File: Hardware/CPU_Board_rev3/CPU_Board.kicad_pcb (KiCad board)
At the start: 2 copper layers, 100 x 70 mm, 116 parts, among them P1 CONN_01X02, P10 CONN_01X02, P11 CONN_01X06, P12 CONN_01X03, P13 CONN_01X01, P14 CONN_01X03, P15 CONN_01X01, P16 CONN_01X01, P17 CONN_01X01, P18 CONN_01X03, P19 CONN_01X01, P2 USB_B, P20 CONN_01X01, P21 CONN_01X06, P22 CONN_01X01, P23 CONN_01X01, P24 CONN_01X06, P25 CONN_01X04, P26 CONN_01X04, P3 CONN_01X04, P4 CONN_01X04, P5 CONN_01X06, P6 CONN_02X12, P7 CONN_01X02, P8 CONN_01X02, P9 CONN_01X02, Q1 Q_PMOS_GSD, Q2 Q_PNP_BCE, Q3 Q_PNP_BCE, U1 STM32F411RETx, U10 MCDTS2-4N, U11 LPS22HB, U12 INA128, U2 NCP1117DT12G, U3 FT232RL, U4 HTS221, U5 INA128, U6 SPBTLE-RF, U7 A2235-H, U8 LSM303AGR, U9 LSM6DSL, Y1 8MHz

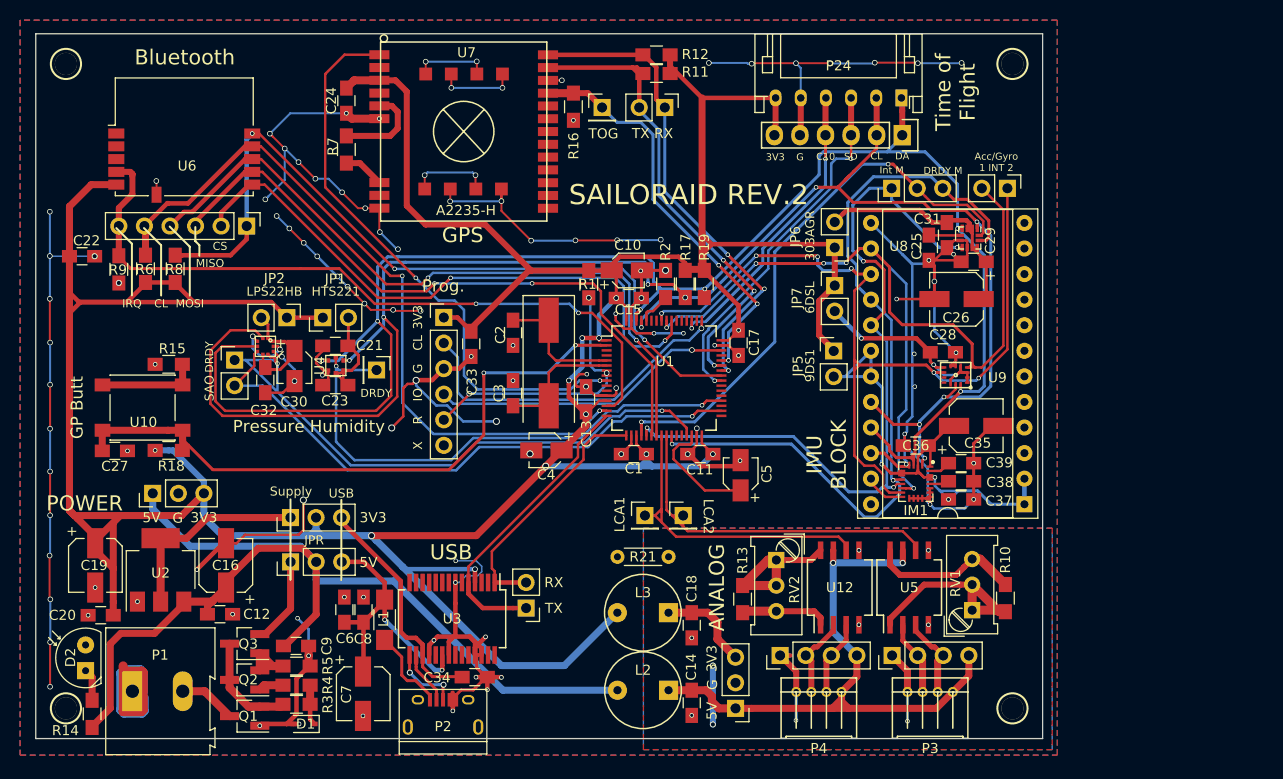
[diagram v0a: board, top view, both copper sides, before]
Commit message: Schematic merge and pcb layout fixes
All minor bugs now fixed, Next up is Footprint and library errors,
followed by actual improvements.
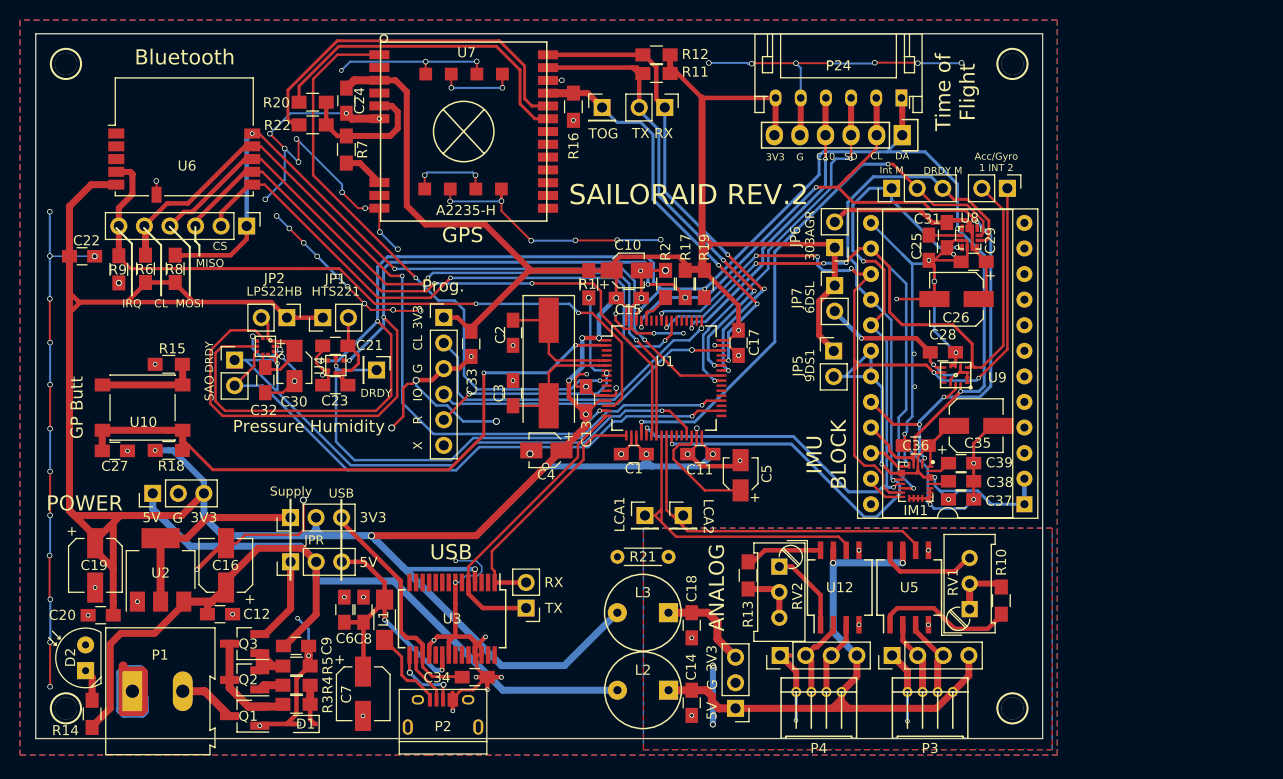
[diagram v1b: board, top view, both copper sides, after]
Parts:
- added R20: 2.2k, Resistors_SMD:R_0805_HandSoldering, F.Cu at (71.0, 109.2)
- added R22: 2.2k, Resistors_SMD:R_0805_HandSoldering, F.Cu at (71.0, 111.4)
- C25: value 220nF -> 100nF
- moved R13 2.41 mm to (114.3, 156.2), turned to 270 degrees
- moved RV2 0.72 mm to (117.4, 155.3)
- moved R10 0.47 mm to (139.4, 158.7)
- moved RV1 0.27 mm to (136.3, 159.5)
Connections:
- net Net-(R7-Pad1) renamed /GPS_Vout
- RV1 pad 1: Net-(R10-Pad1) -> Net-(R10-Pad2)
- RV1 pad 2: Net-(R10-Pad1) -> Net-(R10-Pad2)
- RV1 pad 3: Net-(R10-Pad2) -> Net-(RV1-Pad3)
- RV2 pad 1: Net-(R13-Pad2) -> Net-(RV2-Pad1)
- RV2 pad 3: Net-(R13-Pad1) -> Net-(R13-Pad2)
- U12 pad 1: Net-(R13-Pad1) -> Net-(RV2-Pad1)
- U12 pad 8: Net-(R13-Pad2) -> Net-(R13-Pad1)
- U5 pad 8: Net-(R10-Pad2) -> Net-(RV1-Pad3)
- U7 pad 17: (no net) -> Net-(R20-Pad2)
- U7 pad 18: (no net) -> Net-(R22-Pad2)
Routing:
- net Net-(R22-Pad2): track 0.00 -> 36.7 mm
- net Net-(R20-Pad2): track 0.00 -> 32.9 mm
- net GND: track 444.2 -> 456.9 mm, vias 107 -> 108
- net Net-(RV1-Pad3): track 0.00 -> 9.97 mm
- net Net-(R13-Pad2): track 15.1 -> 5.77 mm
- net Net-(R10-Pad2): track 15.0 -> 5.83 mm
- net Net-(RV2-Pad1): track 0.00 -> 8.21 mm
- net Net-(R10-Pad1): track 20.5 -> 13.8 mm
- net /GPS_Vout: track 9.13 -> 13.8 mm
- net /GPS_NRST: track 57.9 -> 59.3 mm
- net Net-(R13-Pad1): track 8.78 -> 7.67 mm

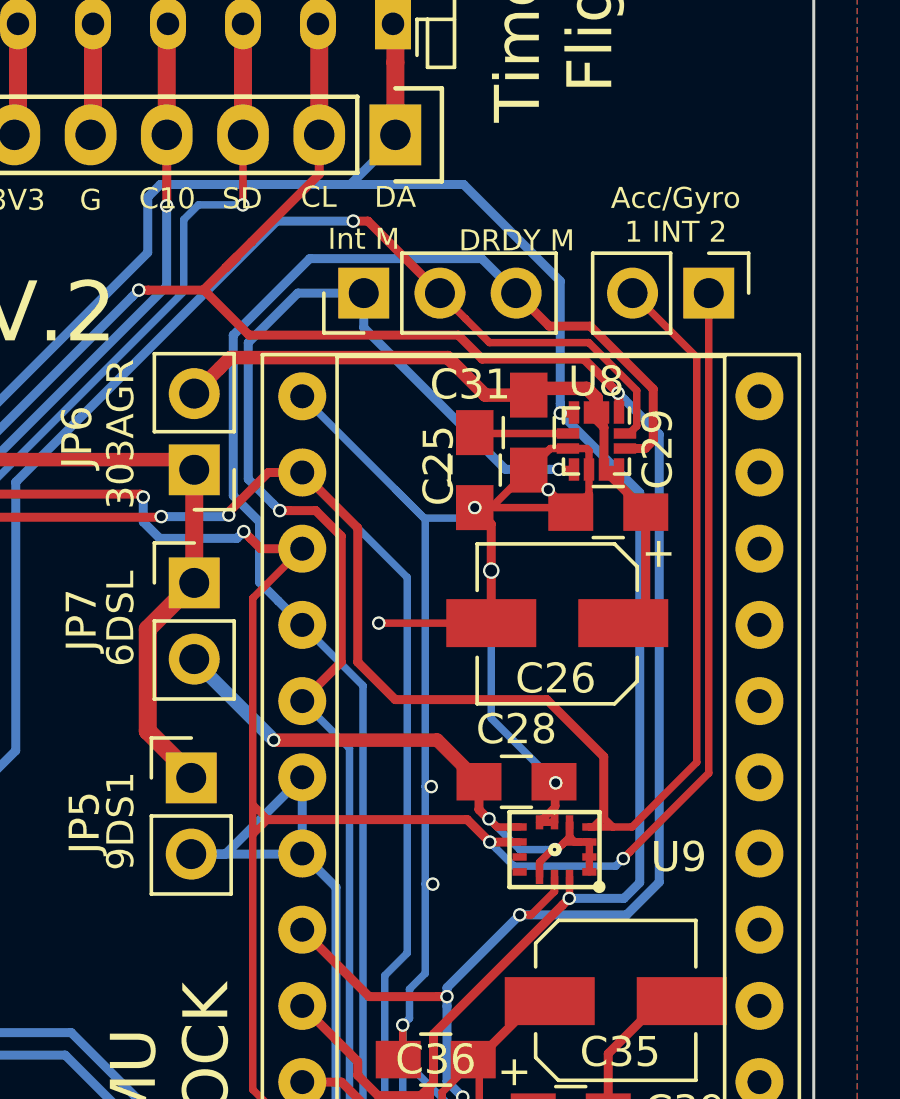
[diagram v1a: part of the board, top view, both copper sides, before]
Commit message: IMU footprints more solderable
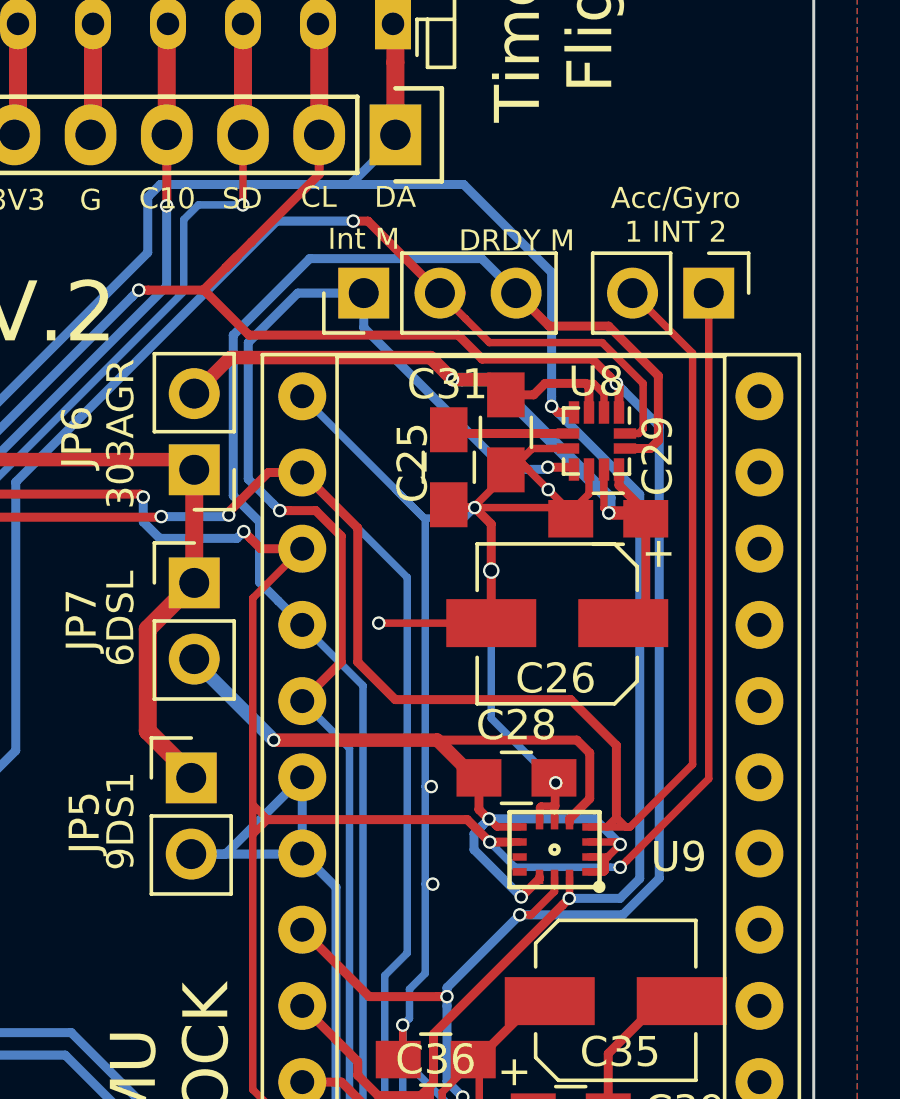
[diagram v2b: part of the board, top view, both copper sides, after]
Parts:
- moved C25 0.87 mm to (131.4, 123.5)
- moved C31 0.76 mm to (133.3, 122.3)
- moved C29 0.22 mm to (136.7, 125.2)
- moved C28 0.13 mm to (133.6, 133.9)
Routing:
- net /LSM6_VDD: track 21.5 -> 34.0 mm, vias 3 -> 4
- net /LSM303_VDD: track 25.3 -> 32.7 mm, vias 0 -> 2
- net Net-(C25-Pad1): track 3.12 -> 4.03 mm
- net /303C_I_XL: track 56.1 -> 56.7 mm
- net /DRDY_Mag: track 79.2 -> 79.8 mm

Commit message: Rev 3 (most stuff)
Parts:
- removed the C35 at (136.9, 141.3)
- removed C36, C37, C39: 100n, Capacitors_SMD:C_0805_HandSoldering
- removed C38: 10n, Capacitors_SMD:C_0805_HandSoldering
- removed IM1: LSM9DS1, FOOTPRINTS:LGA-24L_3x3.5mm_Pitch0.43mm_Handsolder
- removed the JP5 at (122.8, 133.9)
- removed the P6 at (141.7, 149.1)
- added C31: 100n, Capacitors_SMD:C_0805_HandSoldering, F.Cu at (66.4, 143.8)
- added R21: 10k, Resistors_SMD:R_0805_HandSoldering, F.Cu at (71.8, 143.8)
- added U12: LPS22HB, FOOTPRINTS:HLGA-10L_2x2mm_P.5mm_HS, F.Cu at (153.4, 137.4)
- R18: renamed from R1; value 10k -> 1k
- R6: renamed from R17; value 10k -> 5k
- R7: renamed from R19; value 10k -> 5k
- U11: value LPS22HB -> MCDTS2-4N; footprint FOOTPRINTS:HLGA-10L -> Buttons_Switches_SMD:SW_SPST_PTS645
- U4: footprint FOOTPRINTS:HLGA-6L_2x2x.9mm -> FOOTPRINTS:HLGA-6L_2x2x.9mm_HS
- U8: footprint FOOTPRINTS:LGA-12_2x2mm_Pitch0.5mm_Handsolder -> FOOTPRINTS:LGA-12_2x2mm_P.5mm_HS
- U9: footprint FOOTPRINTS:LGA-14 -> FOOTPRINTS:LGA-14_2.5x3mm_P.5_HS
- moved C22 87.1 mm to (160.3, 137.4)
- moved C24 87.1 mm to (160.3, 141.3)
- moved C32 87.1 mm to (156.2, 139.4)
- moved C34 87.1 mm to (153.3, 140.8)
- moved U4 87.1 mm to (160.3, 139.3)
- moved P13 68.0 mm to (129.7, 149.3), turned to 270 degrees
- moved P18 62.0 mm to (137.8, 149.3)
- moved JP4 55.5 mm to (122.8, 141.9), turned to 0 degrees
- moved JP3 51.4 mm to (122.8, 138.3), turned to 180 degrees
- moved R18 33.0 mm to (66.5, 135.2), turned to 180 degrees
- moved U11 6.70 mm to (69.1, 139.5), turned to 180 degrees
- renumbered C34 to C10, C13 to C12, C9 to C13, C15 to C14, C17 to C15, C12 to C16, C16 to C17, C14 to C18, C18 to C21, C21 to C22, C22 to C23, C23 to C24, C24 to C25, C25 to C26, C26 to C27, C27 to C30, C30 to C32, C31 to C33, C32 to C34, C33 to C35, C10 to C9, JP3 to JP1, JP4 to JP2, JP1 to JP3, JP2 to JP4, JP6 to JP5, JP7 to JP6, P7 to P10, P8 to P11, P9 to P12, P10 to P13, P11 to P14, P12 to P15, P13 to P16, P14 to P17, P15 to P18, P16 to P19, P17 to P20, P18 to P21, P19 to P22, P20 to P23, P22 to P24, P23 to P25, P25 to P3, P3 to P4, P26 to P5, P4 to P6, P21 to P7, P24 to P8, P5 to P9, R2 to R1, R8 to R10, R9 to R11, R10 to R12, R11 to R13, R12 to R14, R13 to R15, R20 to R16, R15 to R17, R22 to R19, R3 to R2, R18 to R20, R16 to R22, R21 to R23, R4 to R3, R5 to R4, R14 to R5, R6 to R8, R7 to R9, U12 to U13, U3 to U2, U2 to U3
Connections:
- R18 pad 1: /NRST -> GND
- R18 pad 2: +3V3 -> Net-(R18-Pad2)
- U1 pad 38: (no net) -> /GPS_TOGGLE
- U1 pad 44: /GPS_TOGGLE -> (no net)
- U1 pad 8: /NRST -> /GPS_NRST
- U1 pad 9: /GPS_NRST -> (no net)
- U11 pad 1: /LPS_VDD -> /NRST
- U11 pad 2: /IMU_I2C_CL -> Net-(R18-Pad2)
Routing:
- net /IMU_I2C_CL: track 175.1 -> 76.5 mm, vias 10 -> 5
- net /IMU_I2C_DA: track 169.6 -> 74.4 mm, vias 6 -> 4
- net /DRDY_Mag: track 79.8 -> 9.26 mm, vias 2 -> 0
- net GND: track 457.1 -> 386.7 mm, vias 108 -> 98
- net /INT_Mag: track 75.7 -> 10.2 mm, vias 4 -> 1
- net /LPS_DRDY: track 60.6 -> 0.00 mm, vias 2 -> 0
- net /LSM6DSL_INT2: track 86.2 -> 26.1 mm, vias 6 -> 2
- net /LPS_SA0: track 58.6 -> 0.00 mm, vias 1 -> 0
- net /HTS_DRDY: track 54.0 -> 0.00 mm, vias 2 -> 0
- net /LSM9_CS_A/G: track 53.0 -> 0.00 mm, vias 3 -> 0
- net +3V3: track 396.4 -> 355.6 mm
- net /NRST: track 28.0 -> 0.00 mm, vias 3 -> 0
- net /LSM6DSL_INT1: track 92.9 -> 65.5 mm, vias 5 -> 4
- net (no net): track 24.1 -> 0.00 mm, vias 11 -> 0
- net /HTS_VDD: track 11.5 -> 0.00 mm
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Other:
- board text added: "Press. Humid."
- board text removed: "9DS1"
- board text removed: "IMU BLOCK"
- board text removed: "Pressure Humidity"
